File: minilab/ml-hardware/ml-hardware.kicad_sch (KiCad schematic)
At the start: 21 parts, among them J1 Conn_01x08, J10 WF-0.1, J11 BE_Skt-10_3, J12 BE_Skt-10_1, J13 BE_Skt-10_2, J14 BE-Cnn-10_1, J15 BE-Cnn-10_2, J16 Molex lite-trap, J17 Molex lite-trap, J18 Molex lite-trap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

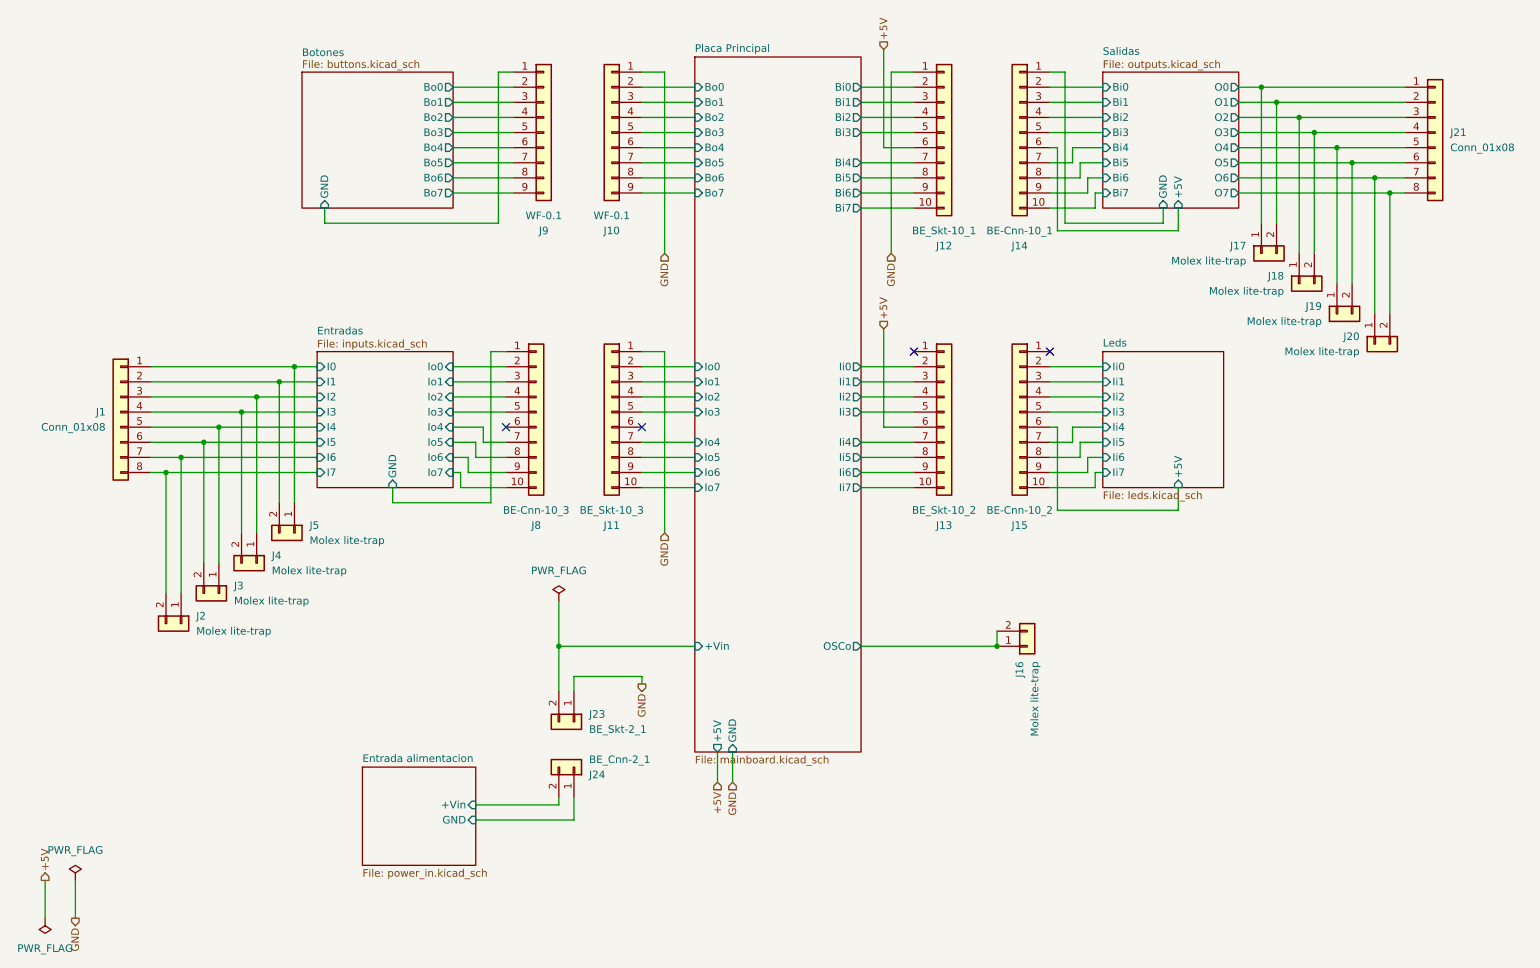
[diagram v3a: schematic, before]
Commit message: minilab: Agrega 2da opc conectores y modelos 3d
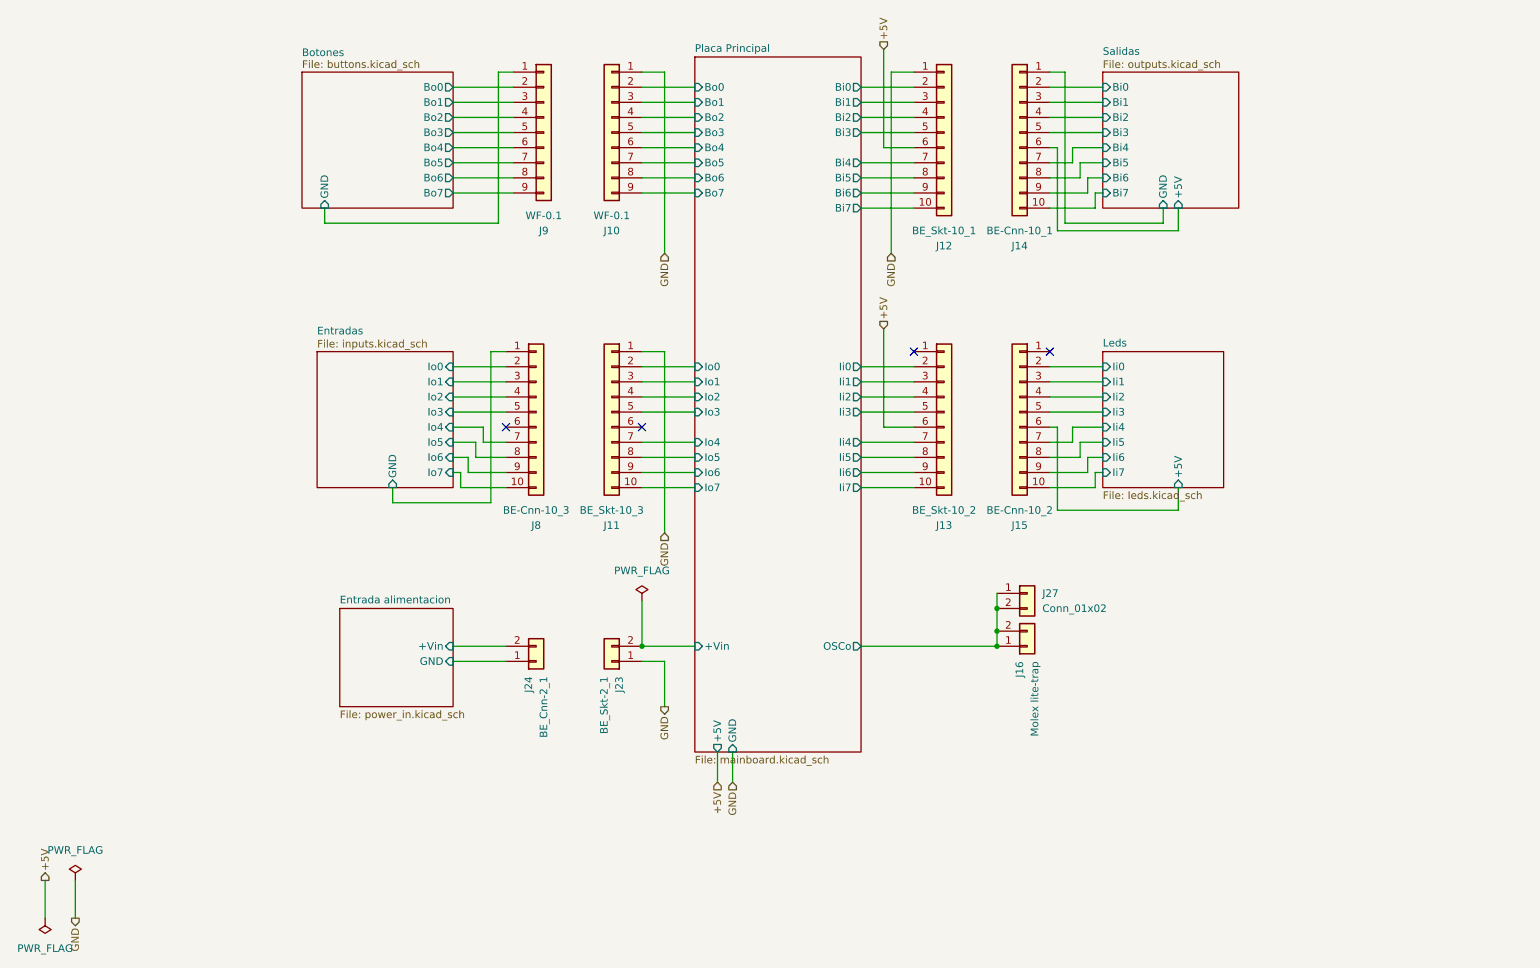
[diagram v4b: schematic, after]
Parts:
- removed J1, J21: Conn_01x08, Connector_PinSocket_2.54mm:PinSocket_1x08_P2.54mm_Horizontal, symbol Connector_Generic:Conn_01x08
- removed J17, J18, J19, J2, J20, J3, J4, J5: Molex lite-trap, Extras:104238-0210, symbol Connector_Generic:Conn_01x02
- added J27: Conn_01x02, Connector_PinSocket_2.54mm:PinSocket_1x02_P2.54mm_Horizontal, symbol Connector_Generic:Conn_01x02
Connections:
- net Placa Principal/OSCo: now also J27.1 (Pin_1), J27.2 (Pin_2)
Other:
- sheet Entradas ports: added none; removed I0, I1, I2, I3, I4, I5, I6, I7
- sheet Salidas ports: added none; removed O0, O1, O2, O3, O4, O5, O6, O7
- moved on the sheet: J23, J24

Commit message: minilab: Corrige huella molex microfit y edge-*-02
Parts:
- J16: footprint Extras:104238-0210 -> Extras:Molex-Lite_trap
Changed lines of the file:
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@@
 			)
 		)
-		(property "Footprint" "Extras:104238-0210"
+		(property "Footprint" "Extras:Molex-Lite_trap"
 			(at 187.96 135.89 0)
 			(effects
